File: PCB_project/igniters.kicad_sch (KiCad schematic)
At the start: 18 parts, among them J10 Conn_01x02, J11 Conn_01x02, Q2 AO3401A, Q4 AO3401A, Q6 AO3400A, Q7 AO3400A

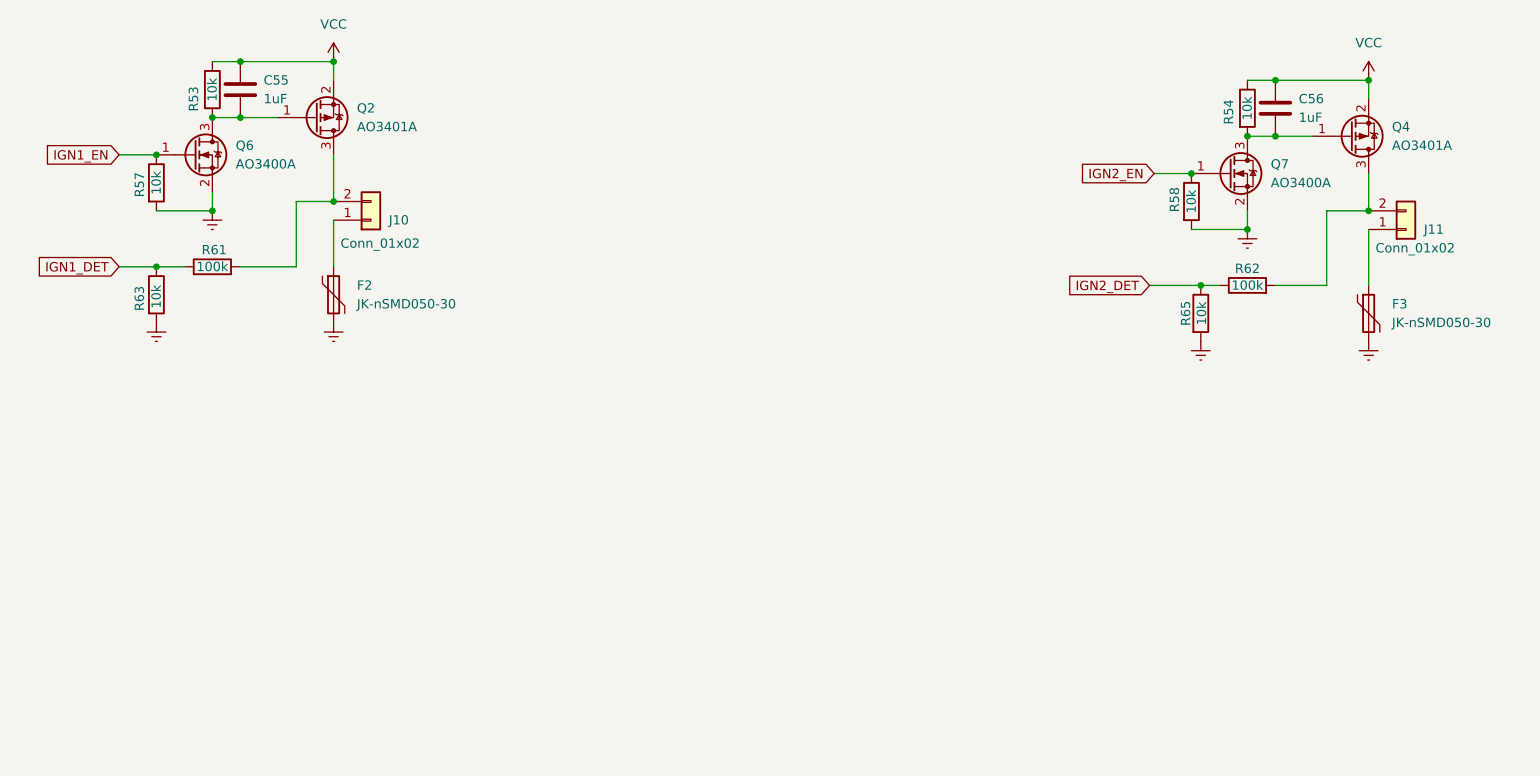
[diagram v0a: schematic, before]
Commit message: Almost ready version. Require more GND vias etc
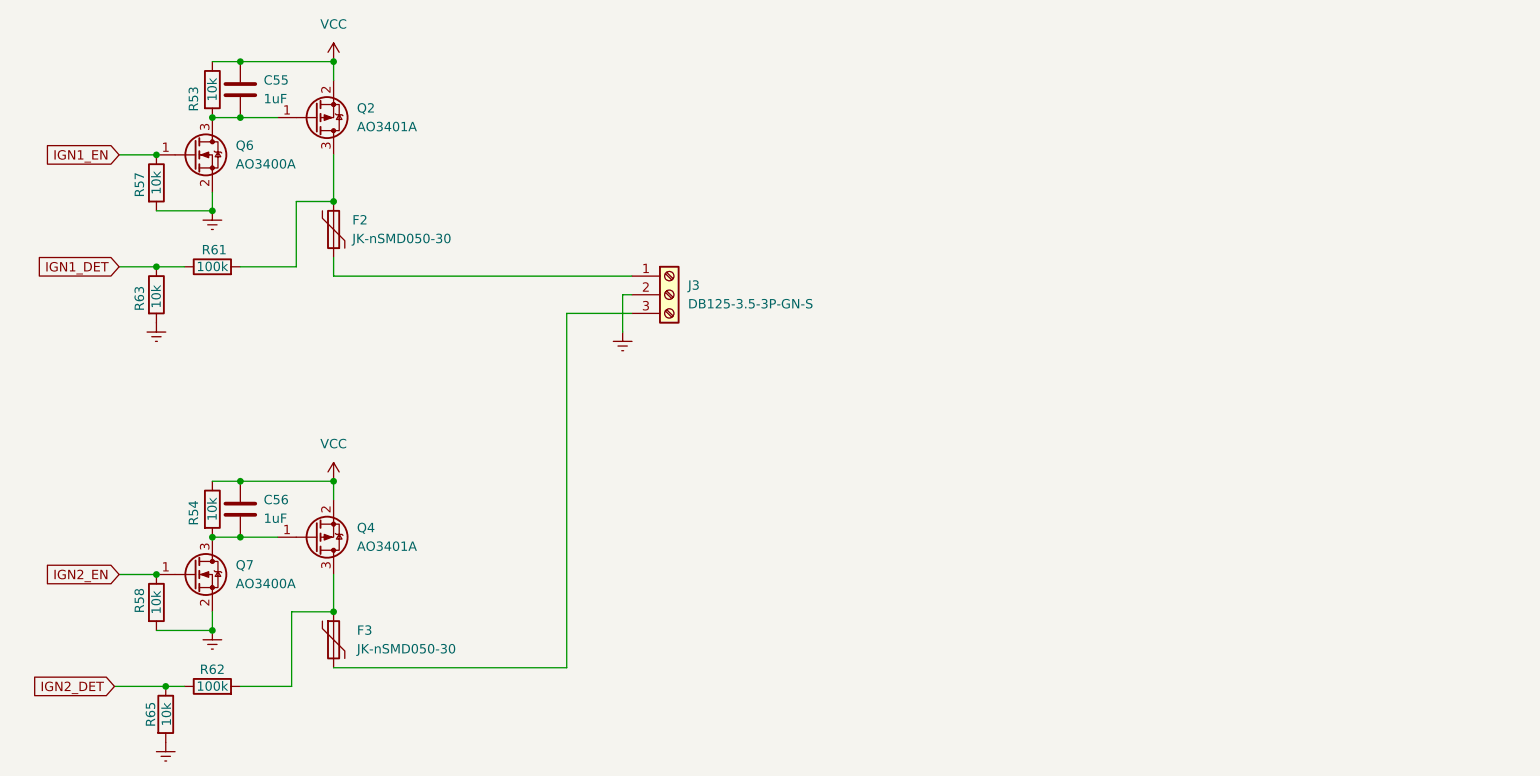
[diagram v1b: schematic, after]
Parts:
- removed J10, J11: Conn_01x02, TerminalBlock_TE-Connectivity:TerminalBlock_TE_282834-2_1x02_P2.54mm_Horizontal, symbol Connector_Generic:Conn_01x02
- added J3: DB125-3.5-3P-GN-S, TerminalBlock_Phoenix:TerminalBlock_Phoenix_PT-1,5-3-3.5-H_1x03_P3.50mm_Horizontal, symbol Connector:Screw_Terminal_01x03
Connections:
- net Earth: now also J3.2 (Pin_2); no longer F2.2, F3.2
- net at Q2.3 (D), R61.2: now also F2.2
- net at Q4.3 (D), R62.2: now also F3.1
- net at F2.1: now also J3.1 (Pin_1)
- new net: F3.2, J3.3 (Pin_3)
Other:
- moved on the sheet: C56, F2, F3, Q4, Q7, R54, R58, R62, R65
